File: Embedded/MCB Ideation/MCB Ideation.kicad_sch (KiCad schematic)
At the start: 25 parts, among them J1 USB, J2 Power, J3 MicroSD, J4 GPIO 0, J5 GPIO 1, J6 GPIO 2, J7 GPIO 3, U1 Sensored, U2 Expansion, U3 Comms Link Expansion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

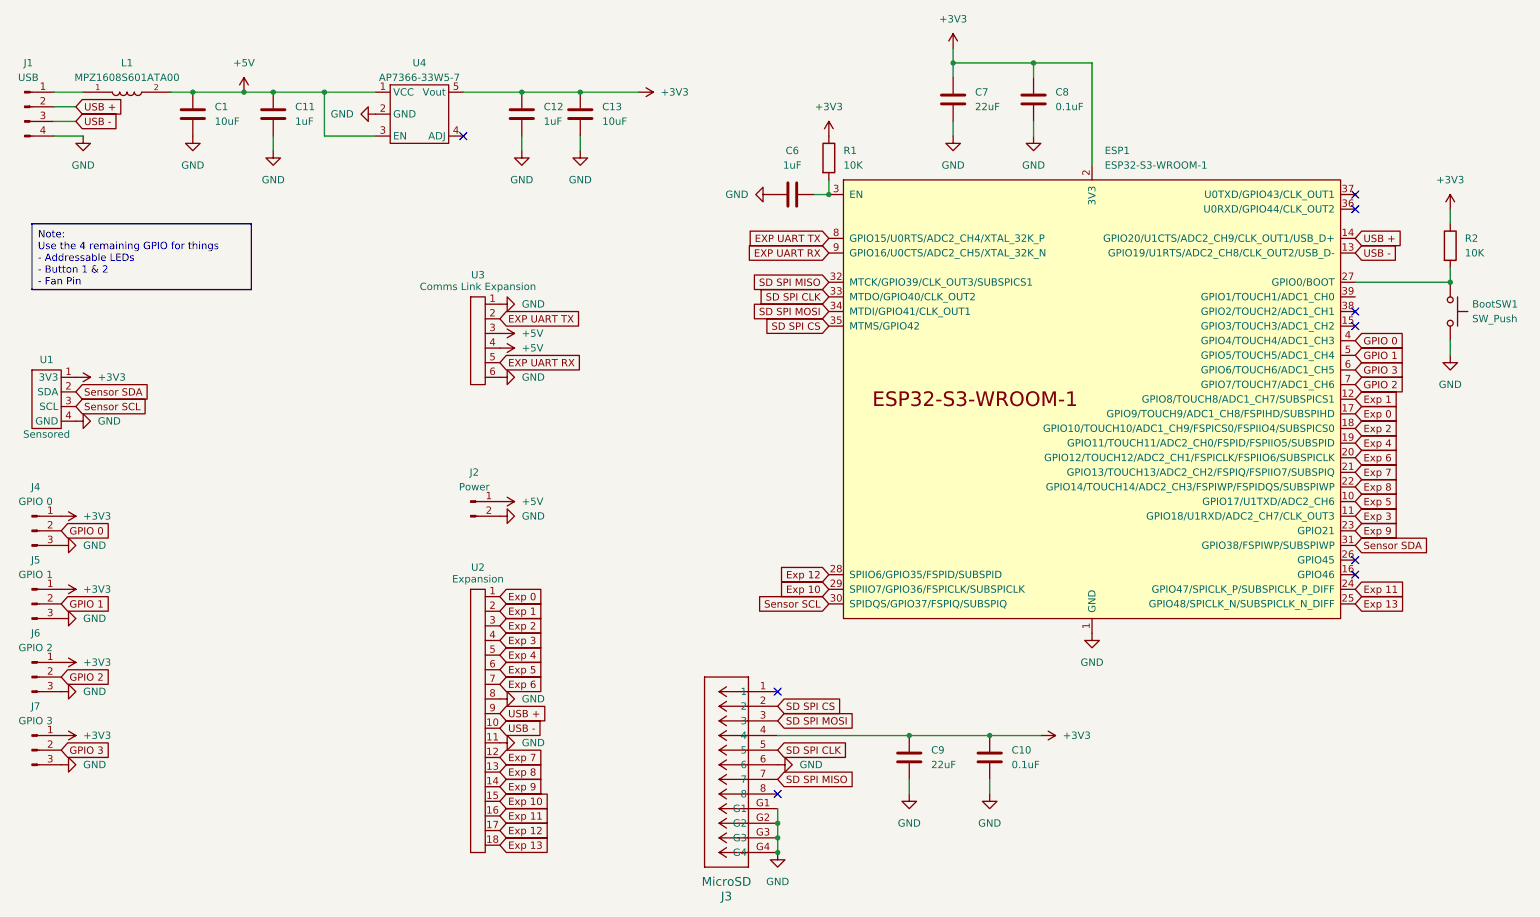
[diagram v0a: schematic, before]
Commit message: Modified GPIO Expansion Pins
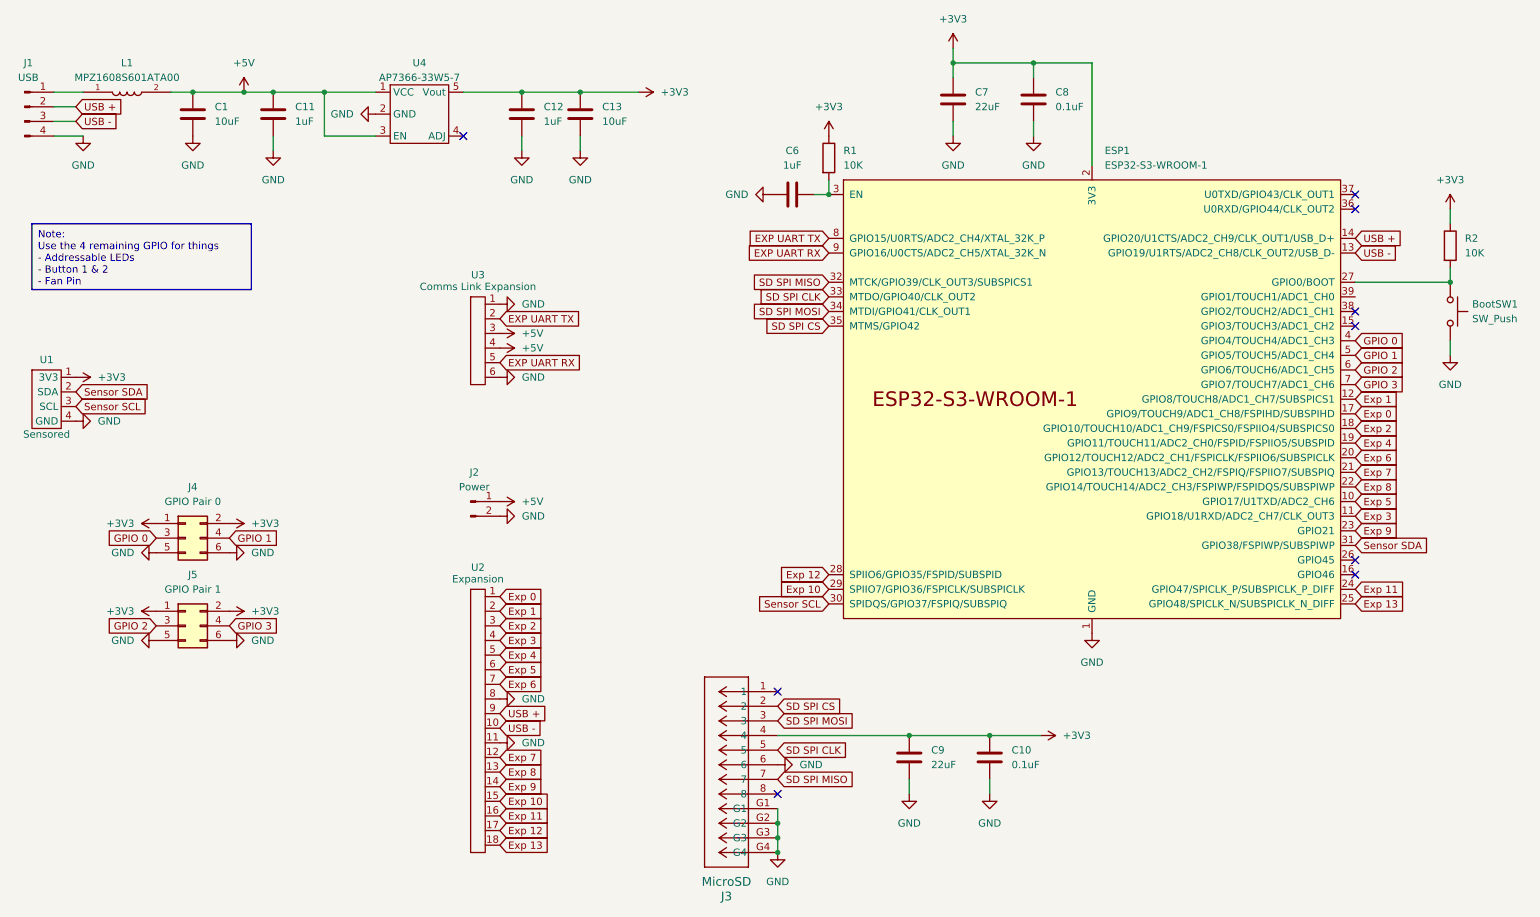
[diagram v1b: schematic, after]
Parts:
- removed J4: GPIO 0, Connector_PinHeader_2.54mm:PinHeader_1x03_P2.54mm_Vertical, symbol Connector:Conn_01x03_Pin
- removed J5: GPIO 1, Connector_PinHeader_2.54mm:PinHeader_1x03_P2.54mm_Vertical, symbol Connector:Conn_01x03_Pin
- removed J6: GPIO 2, Connector_PinHeader_2.54mm:PinHeader_1x03_P2.54mm_Vertical, symbol Connector:Conn_01x03_Pin
- removed J7: GPIO 3, Connector_PinHeader_2.54mm:PinHeader_1x03_P2.54mm_Vertical, symbol Connector:Conn_01x03_Pin
- added J4: GPIO Pair 0, Connector_PinHeader_2.54mm:PinHeader_2x03_P2.54mm_Vertical, symbol Connector_Generic:Conn_02x03_Odd_Even
- added J5: GPIO Pair 1, Connector_PinHeader_2.54mm:PinHeader_2x03_P2.54mm_Vertical, symbol Connector_Generic:Conn_02x03_Odd_Even
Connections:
- net +3V3: now also J4.1 (Pin_1), J4.2 (Pin_2), J5.1 (Pin_1), J5.2 (Pin_2)
- net GND: now also J4.5 (Pin_5), J4.6 (Pin_6), J5.5 (Pin_5), J5.6 (Pin_6)
- net GPIO 0: now also J4.3 (Pin_3)
- net GPIO 1: now also J4.4 (Pin_4)
- net GPIO 2: now also ESP1.6 (GPIO6/TOUCH6/ADC1_CH5), J5.3 (Pin_3); no longer ESP1.7 (GPIO7/TOUCH7/ADC1_CH6)
- net GPIO 3: now also ESP1.7 (GPIO7/TOUCH7/ADC1_CH6), J5.4 (Pin_4); no longer ESP1.6 (GPIO6/TOUCH6/ADC1_CH5)
